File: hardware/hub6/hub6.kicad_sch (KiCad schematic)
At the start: 10 parts, among them J1 plate 1, J2 plate 2, J3 plate 3, J4 plate 4, J5 plate 5, J6 base, J7 XIAO D0-D6, J8 XIAO D7-5V, U2 XIAO ESP32S3

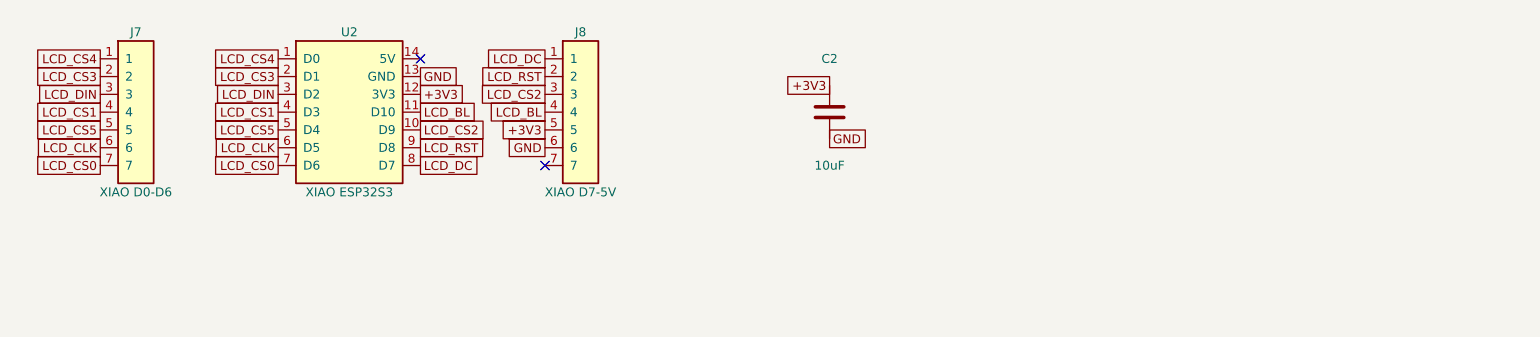
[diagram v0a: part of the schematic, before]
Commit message: hub6: add the 74HC138 back and widen the board to 25 mm to the edge
The cup's inside (measured from lcd_cup.stl) allows a hexagon 25 mm from
centre to edge when the board sits about 22 mm up, so the board grows from
22.5 mm and the 74HC138 goes under the XIAO again. A0, A1, A2 take D7, D8,
D9 and the six chip selects come from the decoder: U1's outputs run on In2
inside radius 12.4 mm through the gaps between socket pads, then up to F.Cu
at a lane via per header. assign.py now plans this (visibility graph on
In2) and writes layout.json, which make.py and the README follow. D3, D6
and D10 are free. ERC, DRC with schematic parity, and 14 tests pass.

Claude-Session: https://claude.ai/code/session_01WVeYczw2dnncq6csD58pZW
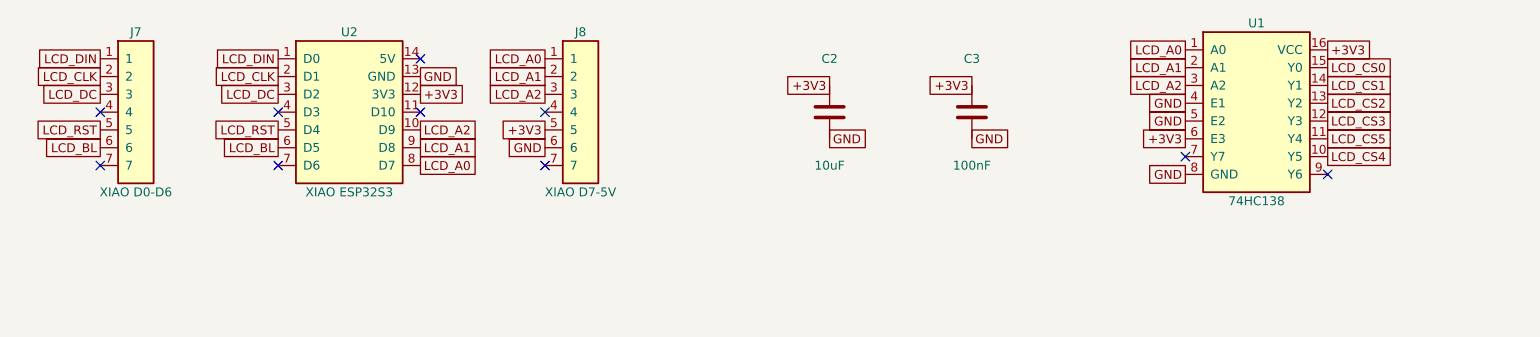
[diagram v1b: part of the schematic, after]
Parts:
- added C3: 100nF, Capacitor_SMD:C_0603_1608Metric, symbol Device:C
- added U1: 74HC138, Package_SO:SOIC-16_3.9x9.9mm_P1.27mm, symbol dodecahedron-earth:74HC138
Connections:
- net +3V3: now also C3.1, U1.16 (VCC), U1.6 (E3)
- net GND: now also C3.2, U1.4 (E1), U1.5 (E2), U1.8 (GND)
- net LCD_BL: now also J7.6, U2.6 (D5); no longer J8.4, U2.11 (D10)
- net LCD_CLK: now also J7.2, U2.2 (D1); no longer J7.6, U2.6 (D5)
- net LCD_CS0: now also U1.15 (Y0); no longer J7.7, U2.7 (D6)
- net LCD_CS1: now also U1.14 (Y1); no longer J7.4, U2.4 (D3)
- net LCD_CS2: now also U1.13 (Y2); no longer J8.3, U2.10 (D9)
- net LCD_CS3: now also U1.12 (Y3); no longer J7.2, U2.2 (D1)
- net LCD_CS4: now also U1.10 (Y5); no longer J7.1, U2.1 (D0)
- net LCD_CS5: now also U1.11 (Y4); no longer J7.5, U2.5 (D4)
- net LCD_DC: now also J7.3, U2.3 (D2); no longer J8.1, U2.8 (D7)
- net LCD_DIN: now also J7.1, U2.1 (D0); no longer J7.3, U2.3 (D2)
- net LCD_RST: now also J7.5, U2.5 (D4); no longer J8.2, U2.9 (D8)
- new net LCD_A0: J8.1, U1.1 (A0), U2.8 (D7)
- new net LCD_A1: J8.2, U1.2 (A1), U2.9 (D8)
- new net LCD_A2: J8.3, U1.3 (A2), U2.10 (D9)
- no-connect marks 2 -> 10

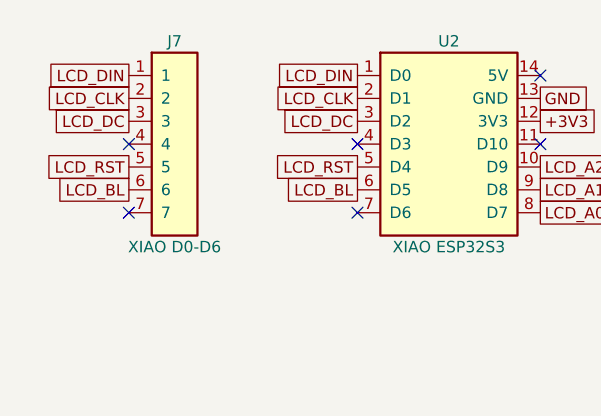
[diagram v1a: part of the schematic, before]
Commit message: hub6: pentagon board with the display cables soldered straight in
The board becomes a regular pentagon (26 mm to the edge) whose edges face
the cup's five side plates one to one, instead of a hexagon whose corners
came close to the wall. The PH2.0 headers go: the cables (PH2.0 at the
display, bare 26 AWG wire here) are cut to length and soldered into rows
of eight holes, so no short double-ended cable has to be bought or crimped.
The side displays' rows run along the edges with two slots each for a
cable tie; the base display's row runs just outside the XIAO's right
socket row, over its plug, so its cable comes straight up from below and
no second board is needed.

The shared signals move to D0, D1, D3, D4, D5, level with the base row's
pins 3, 4, 6, 7, 8, and reach the rings (now 17.6 to 20.8 mm) through it.
assign.py now chooses the ring order (4 of 120 clear the stubs) and the
chip-select lanes for the new geometry. ERC, DRC and 17 tests pass.
fab.py also copies the upload files into fab6/.

Claude-Session: https://claude.ai/code/session_01WVeYczw2dnncq6csD58pZW
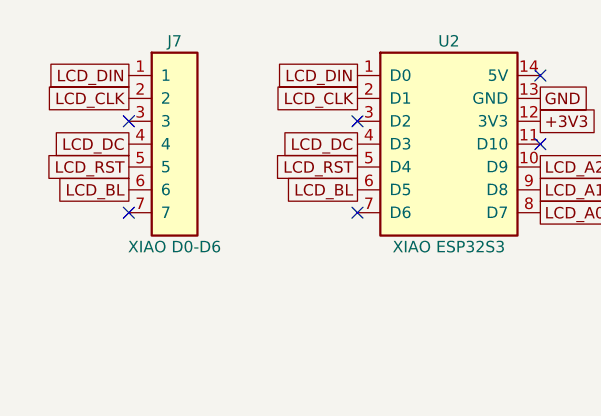
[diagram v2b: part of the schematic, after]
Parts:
- removed J1: plate 1, dodecahedron-earth:PH2.0_8P_Vertical_THT_C157974, symbol dodecahedron-earth:PH2.0_8P
- removed J2: plate 2, dodecahedron-earth:PH2.0_8P_Vertical_THT_C157974, symbol dodecahedron-earth:PH2.0_8P
- removed J3: plate 3, dodecahedron-earth:PH2.0_8P_Vertical_THT_C157974, symbol dodecahedron-earth:PH2.0_8P
- removed J4: plate 4, dodecahedron-earth:PH2.0_8P_Vertical_THT_C157974, symbol dodecahedron-earth:PH2.0_8P
- removed J5: plate 5, dodecahedron-earth:PH2.0_8P_Vertical_THT_C157974, symbol dodecahedron-earth:PH2.0_8P
- removed J6: base, dodecahedron-earth:PH2.0_8P_Vertical_THT_C157974, symbol dodecahedron-earth:PH2.0_8P
- added J1: plate 1, dodecahedron-earth:Wire_1x08_P2.54_Tie, symbol dodecahedron-earth:Cable_8P
- added J2: plate 2, dodecahedron-earth:Wire_1x08_P2.54_Tie, symbol dodecahedron-earth:Cable_8P
- added J3: plate 3, dodecahedron-earth:Wire_1x08_P2.54_Tie, symbol dodecahedron-earth:Cable_8P
- added J4: plate 4, dodecahedron-earth:Wire_1x08_P2.54_Tie, symbol dodecahedron-earth:Cable_8P
- added J5: plate 5, dodecahedron-earth:Wire_1x08_P2.54_Tie, symbol dodecahedron-earth:Cable_8P
- added J6: base, dodecahedron-earth:Wire_1x08_P2.54, symbol dodecahedron-earth:Cable_8P
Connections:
- net +3V3: now also J1.1 (VCC), J2.1 (VCC), J3.1 (VCC), J4.1 (VCC), J5.1 (VCC), J6.1 (VCC)
- net GND: now also J1.2 (GND), J2.2 (GND), J3.2 (GND), J4.2 (GND), J5.2 (GND), J6.2 (GND)
- net LCD_BL: now also J1.8 (BL), J2.8 (BL), J3.8 (BL), J4.8 (BL), J5.8 (BL), J6.8 (BL)
- net LCD_CLK: now also J1.4 (CLK), J2.4 (CLK), J3.4 (CLK), J4.4 (CLK), J5.4 (CLK), J6.4 (CLK)
- net LCD_CS0: now also J1.5 (CS)
- net LCD_CS1: now also J2.5 (CS)
- net LCD_CS2: now also J3.5 (CS)
- net LCD_CS3: now also J4.5 (CS)
- net LCD_CS4: now also J5.5 (CS)
- net LCD_CS5: now also J6.5 (CS)
- net LCD_DC: now also J7.4, U2.4 (D3), J1.6 (DC), J2.6 (DC), J3.6 (DC), J4.6 (DC), J5.6 (DC), J6.6 (DC); no longer J7.3, U2.3 (D2)
- net LCD_DIN: now also J1.3 (DIN), J2.3 (DIN), J3.3 (DIN), J4.3 (DIN), J5.3 (DIN), J6.3 (DIN)
- net LCD_RST: now also J1.7 (RST), J2.7 (RST), J3.7 (RST), J4.7 (RST), J5.7 (RST), J6.7 (RST)

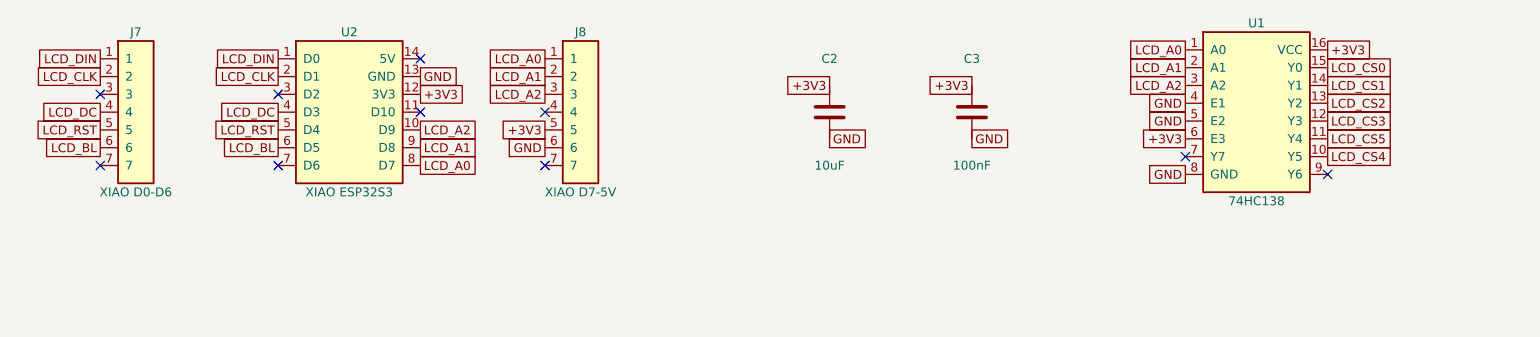
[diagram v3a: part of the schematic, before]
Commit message: hub6 rev C, board A: two layers, the XIAO moved to a board of its own
With the XIAO and its sockets gone from the middle, two layers carry everything: B.Cu
has only the rings (3V3 innermost, then the five shared signals) and GND round them;
F.Cu has straight lines that cross the rings freely. The side rows reach the rings by
radial stubs; J7 (a 2x5 header underneath, to board B) and the base display's holes
(now a 2x4 block, numbered like a DIP-8, over the base plug) reach them through two
of the pentagon's corners. The chip selects run in to the 74HC138 at the centre,
each to the output that lets no line cross another (P1 Y2, P2 Y1, P3 Y0, P4 Y5,
P5 Y4, base Y3). assign.py and layout.json are gone: nothing is left to search.
ERC and DRC clean, 14 tests. README still describes rev B; it follows with board B.

Claude-Session: https://claude.ai/code/session_01WVeYczw2dnncq6csD58pZW
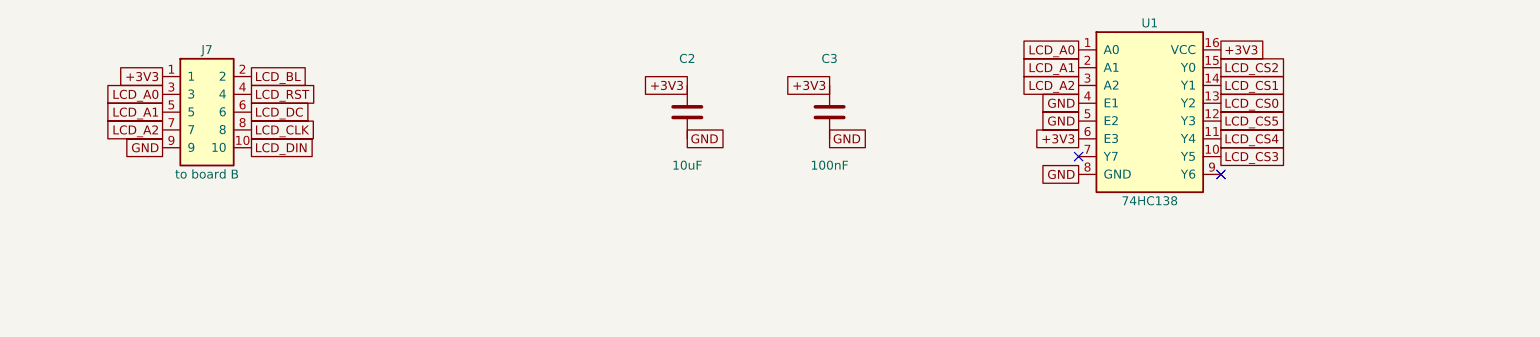
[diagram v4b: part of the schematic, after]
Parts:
- removed J7: XIAO D0-D6, Connector_PinSocket_2.54mm:PinSocket_1x07_P2.54mm_Vertical, symbol dodecahedron-earth:Socket_1x07
- removed J8: XIAO D7-5V, Connector_PinSocket_2.54mm:PinSocket_1x07_P2.54mm_Vertical, symbol dodecahedron-earth:Socket_1x07
- removed U2: XIAO ESP32S3, symbol dodecahedron-earth:XIAO_ESP32S3
- added J7: to board B, Connector_PinHeader_2.54mm:PinHeader_2x05_P2.54mm_Vertical, symbol dodecahedron-earth:Header_2x05
- J6: footprint dodecahedron-earth:Wire_1x08_P2.54 -> dodecahedron-earth:Wire_2x04_P2.54
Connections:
- net +3V3: now also J7.1
- net GND: now also J7.9
- net LCD_A0: now also J7.3
- net LCD_A1: now also J7.5
- net LCD_A2: now also J7.7
- net LCD_BL: now also J7.2
- net LCD_CLK: now also J7.8
- net LCD_CS0: now also U1.13 (Y2); no longer U1.15 (Y0)
- net LCD_CS2: now also U1.15 (Y0); no longer U1.13 (Y2)
- net LCD_CS3: now also U1.10 (Y5); no longer U1.12 (Y3)
- net LCD_CS4: now also U1.11 (Y4); no longer U1.10 (Y5)
- net LCD_CS5: now also U1.12 (Y3); no longer U1.11 (Y4)
- net LCD_DC: now also J7.6
- net LCD_DIN: now also J7.10
- net LCD_RST: now also J7.4
- no-connect marks 10 -> 2
